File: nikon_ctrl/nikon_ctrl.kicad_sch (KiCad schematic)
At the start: 34 parts, among them J1 USB3_A, J2 SJ-2523-SMT-TR, J3 Conn_01x03, Q1 VOM617A-4T, Q2 VOM617A-4T, Q3 BC817, Q4 BC817, Q5 BC817, Q6 BC817, U1 FT230XQ, U2 TPD2EUSB30

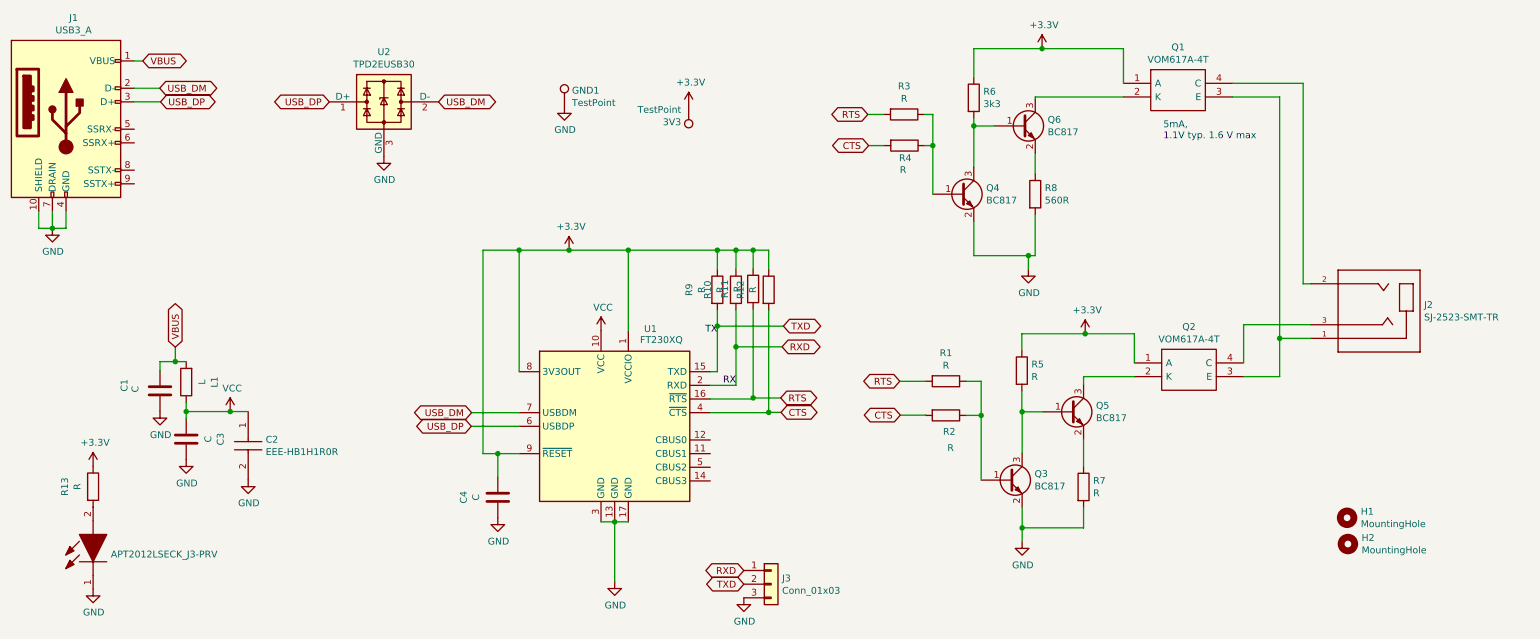
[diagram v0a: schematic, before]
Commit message: updated component values
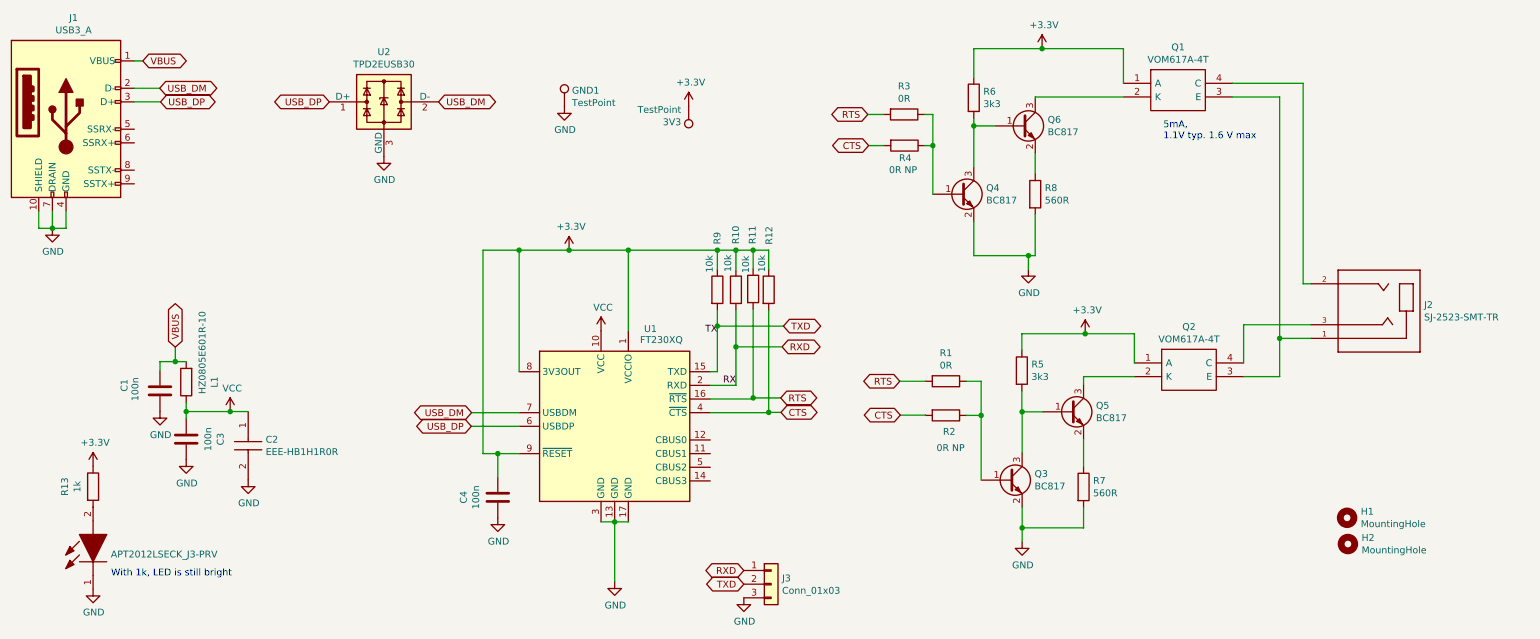
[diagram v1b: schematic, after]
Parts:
- C1, C3, C4: value C -> 100n
- L1: value L -> HZ0805E601R-10
- R1, R3: value R -> 0R
- R10, R11, R12, R9: value R -> 10k
- R13: value R -> 1k
- R2, R4: value R -> 0R NP
- R5: value R -> 3k3
- R7: value R -> 560R
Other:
- note added: "With 1k, LED is still bright"
